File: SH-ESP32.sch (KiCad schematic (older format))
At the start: 21 parts

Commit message: Update according to comments
Also add missing connectors and update the fuses
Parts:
- removed C? (x2): 0.1u/50V, symbol Device:C_Small
- removed C?: 100n, symbol Device:C
- removed C?: 22uF/6.3V, Capacitor_SMD:C_0805_2012Metric, symbol Device:C
- removed D?: RED LED, symbol Device:LED
- removed D?: BLUE LED, symbol Device:LED
- removed J? (x2): Conn_01x15, symbol Connector_Generic:Conn_01x15
- removed R? (x7): 0R, symbol Device:R
- removed R?: 10k, symbol Device:R
- removed R? (x2): 2k, symbol Device:R
- removed SW? (x2): SW_Push, symbol Switch:SW_Push
- removed U?: ESP32-WROOM-32D, RF_Module:ESP32-WROOM-32, symbol RF_Module:ESP32-WROOM-32D
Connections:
- net labels added: BOOT, CAN_RX, CAN_TX, DQ, LED, OPTO_IN1, OPTO_OUT1, RESET, SCL, SDA, USB_RXD, USB_TXD, Vin
- net labels removed: +3.3V, EN, EXT_5V, GND, IO0, IO12, IO13, IO14, IO15, IO16, IO17, IO18, IO19, IO2, IO21, IO22, IO23, IO25, IO26, IO27, IO32, IO33, IO34, IO35, IO4, IO5, RXD0, SCK, SCS, SDI, SDO, SENSOR_VN, SENSOR_VP, SHD, SWP, TXD0
- wire segments 51 -> 28
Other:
- note removed: "Boot"
- note removed: "FIXME: All IO pins are provisional"
- note removed: "Reset"

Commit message: Rough PCB layout
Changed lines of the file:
@@
 F9 "OPTO_IN1" I R 6150 3150 50
 F10 "OPTO_OUT1" I R 6150 3300 50
-F11 "LED" I L 4800 2950 50
-F12 "RESET" I L 4800 2650 50
-F13 "BOOT" I L 4800 2800 50
+F11 "LED" I L 4800 2900 50
+F12 "RESET" I L 4800 2600 50
+F13 "BOOT" I L 4800 2750 50
 $EndSheet
 $Sheet
@@
 F0 "Power input" 50
 F1 "power-input.sch" 50
-F2 "Vin" I R 2250 1150 50
 $EndSheet
 $Sheet
@@
 F2 "TXD" I R 2250 2350 50
 F3 "RXD" I R 2250 2500 50
-F4 "BOOT" I R 2250 3250 50
-F5 "RESET" I R 2250 3100 50
+F4 "BOOT" I R 2250 3000 50
+F5 "RESET" I R 2250 2850 50
 $EndSheet
 $Sheet
@@
 F2 "CAN_RX" I L 9300 1150 50
 F3 "CAN_TX" I L 9300 1300 50
-F4 "Vin" I L 9300 1600 50
 $EndSheet
 $Sheet
@@
 F3 "OUT1" I L 9300 4650 50
 $EndSheet
-Text Label 2350 3250 0    50   ~ 0
+Text Label 2350 3000 0    50   ~ 0
 BOOT
-Text Label 2350 3100 0    50   ~ 0
+Text Label 2350 2850 0    50   ~ 0
 RESET
 Wire Wire Line
-	2350 3250 2250 3250
+	2350 3000 2250 3000
 Wire Wire Line
-	2350 3100 2250 3100
+	2350 2850 2250 2850
 Wire Wire Line
 	9300 2300 9200 2300
@@
 Wire Wire Line
 	2350 4250 2250 4250
-Text Label 4700 2800 2    50   ~ 0
+Text Label 4700 2750 2    50   ~ 0
 BOOT
-Text Label 4700 2650 2    50   ~ 0
+Text Label 4700 2600 2    50   ~ 0
 RESET
 Wire Wire Line
-	4700 2800 4800 2800
+	4700 2750 4800 2750
 Wire Wire Line
-	4700 2650 4800 2650
-Text Label 4700 2950 2    50   ~ 0
+	4700 2600 4800 2600
+Text Label 4700 2900 2    50   ~ 0
 LED
 Wire Wire Line
-	4700 2950 4800 2950
+	4700 2900 4800 2900
 Text Label 6250 2150 0    50   ~ 0
 CAN_TX
@@
 Wire Wire Line
 	6250 3300 6150 3300
-Text Label 9200 1600 2    50   ~ 0
-Vin
-Wire Wire Line
-	9300 1600 9200 1600
-Text Label 2350 1150 0    50   ~ 0
-Vin
-Wire Wire Line
-	2250 1150 2350 1150
 $EndSCHEMATC

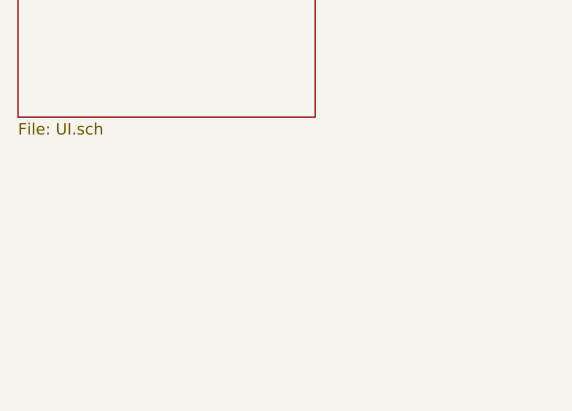
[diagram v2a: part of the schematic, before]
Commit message: Added decoupling caps next to trace vias and copper fill islands
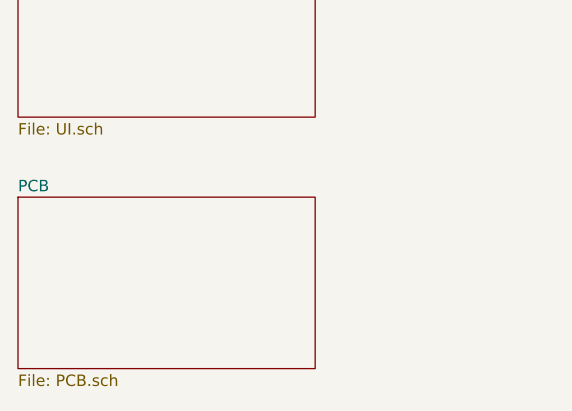
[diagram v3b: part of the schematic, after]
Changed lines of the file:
@@
 $Descr A4 11693 8268
 encoding utf-8
-Sheet 1 9
+Sheet 1 10
 Title "Sailor Hat for ESP32"
 Date ""
@@
 Wire Wire Line
 	6250 3300 6150 3300
+$Sheet
+S 950  5150 1300 750
+U 5FC0C355
+F0 "PCB" 50
+F1 "PCB.sch" 50
+$EndSheet
 $EndSCHEMATC

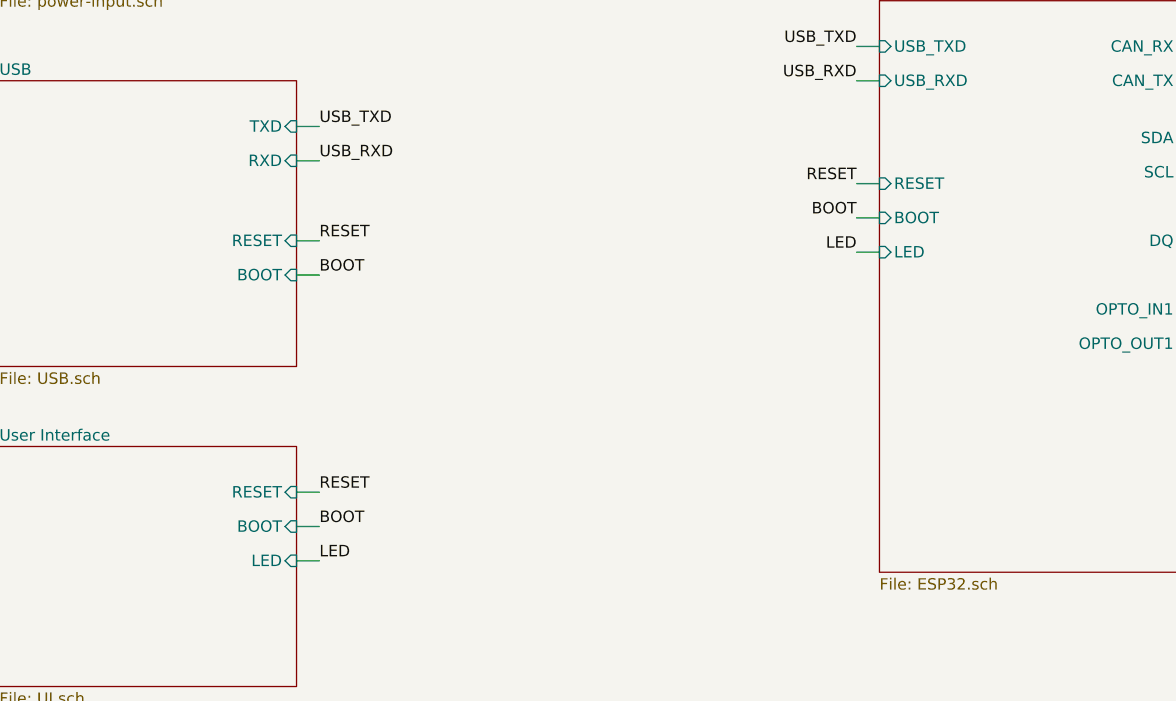
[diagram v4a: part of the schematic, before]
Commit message: Initial version with 40Pin header for Ethernet and re-route.
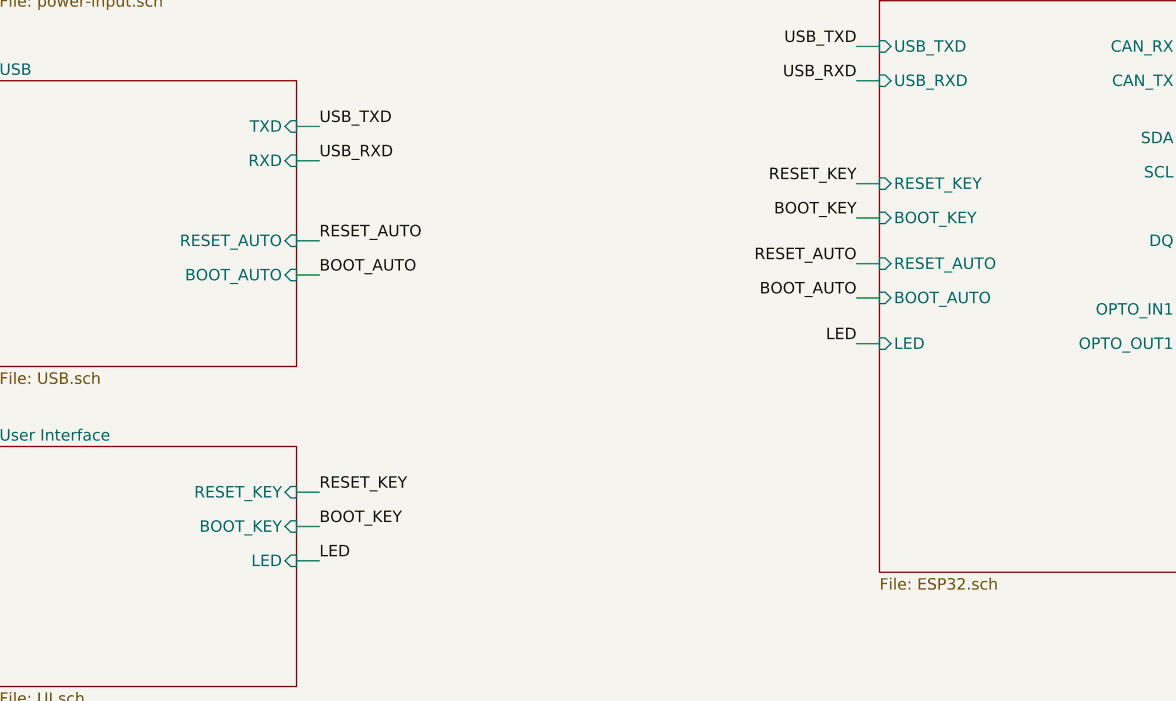
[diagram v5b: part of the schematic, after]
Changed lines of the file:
@@
 $EndDescr
-$Sheet
-S 4800 1800 1350 2500
-U 5FC3847D
-F0 "ESP32" 50
-F1 "ESP32.sch" 50
-F2 "USB_TXD" I L 4800 2000 50
-F3 "USB_RXD" I L 4800 2150 50
-F4 "CAN_RX" I R 6150 2000 50
-F5 "CAN_TX" I R 6150 2150 50
-F6 "SDA" I R 6150 2400 50
-F7 "SCL" I R 6150 2550 50
-F8 "DQ" I R 6150 2850 50
-F9 "OPTO_IN1" I R 6150 3150 50
-F10 "OPTO_OUT1" I R 6150 3300 50
-F11 "LED" I L 4800 2900 50
-F12 "RESET" I L 4800 2600 50
-F13 "BOOT" I L 4800 2750 50
-$EndSheet
 $Sheet
 S 950  950  1300 800
@@
 F2 "TXD" I R 2250 2350 50
 F3 "RXD" I R 2250 2500 50
-F4 "BOOT" I R 2250 3000 50
-F5 "RESET" I R 2250 2850 50
+F4 "BOOT_AUTO" I R 2250 3000 50
+F5 "RESET_AUTO" I R 2250 2850 50
 $EndSheet
 $Sheet
@@
 F0 "User Interface" 50
 F1 "UI.sch" 50
-F2 "RESET" I R 2250 3950 50
-F3 "BOOT" I R 2250 4100 50
+F2 "RESET_KEY" I R 2250 3950 50
+F3 "BOOT_KEY" I R 2250 4100 50
 F4 "LED" I R 2250 4250 50
 $EndSheet
@@
 $EndSheet
 Text Label 2350 3000 0    50   ~ 0
-BOOT
+BOOT_AUTO
 Text Label 2350 2850 0    50   ~ 0
-RESET
+RESET_AUTO
 Wire Wire Line
 	2350 3000 2250 3000
@@
 	4800 2150 4700 2150
 Text Label 2350 4100 0    50   ~ 0
-BOOT
+BOOT_KEY
 Text Label 2350 3950 0    50   ~ 0
-RESET
+RESET_KEY
 Wire Wire Line
 	2350 4100 2250 4100
@@
 	2350 4250 2250 4250
 Text Label 4700 2750 2    50   ~ 0
-BOOT
+BOOT_KEY
 Text Label 4700 2600 2    50   ~ 0
-RESET
+RESET_KEY
 Wire Wire Line
 	4700 2750 4800 2750
 Wire Wire Line
 	4700 2600 4800 2600
-Text Label 4700 2900 2    50   ~ 0
-LED
-Wire Wire Line
-	4700 2900 4800 2900
 Text Label 6250 2150 0    50   ~ 0
 CAN_TX
@@
 F1 "PCB.sch" 50
 $EndSheet
+Wire Wire Line
+	4700 3300 4800 3300
+Text Label 4700 3300 2    50   ~ 0
+LED
+Text Label 4700 2950 2    50   ~ 0
+RESET_AUTO
+Text Label 4700 3100 2    50   ~ 0
+BOOT_AUTO
+Wire Wire Line
+	4700 2950 4800 2950
+$Sheet
+S 4800 1800 1350 2500
+U 5FC3847D
+F0 "ESP32" 50
+F1 "ESP32.sch" 50
+F2 "USB_TXD" I L 4800 2000 50
+F3 "USB_RXD" I L 4800 2150 50
+F4 "CAN_RX" I R 6150 2000 50
+F5 "CAN_TX" I R 6150 2150 50
+F6 "SDA" I R 6150 2400 50
+F7 "SCL" I R 6150 2550 50
+F8 "DQ" I R 6150 2850 50
+F9 "OPTO_IN1" I R 6150 3150 50
+F10 "OPTO_OUT1" I R 6150 3300 50
+F11 "LED" I L 4800 3300 50
+F12 "RESET_KEY" I L 4800 2600 50
+F13 "BOOT_KEY" I L 4800 2750 50
+F14 "RESET_AUTO" I L 4800 2950 50
+F15 "BOOT_AUTO" I L 4800 3100 50
+$EndSheet
+Wire Wire Line
+	4700 3100 4800 3100
 $EndSCHEMATC
